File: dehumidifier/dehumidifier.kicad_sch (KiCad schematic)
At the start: 13 parts, among them J1 Conn_01x04_Pin, J2 Conn_01x02_Pin, J3 Conn_01x03_Pin, J4 Conn_01x03_Pin, J5 Barrel_Jack_Switch, M1 Fan, Q1 Q_NMOS_GDS, U1 SeeeduinoXIAO, U2 DHT11, U3 DS18B20

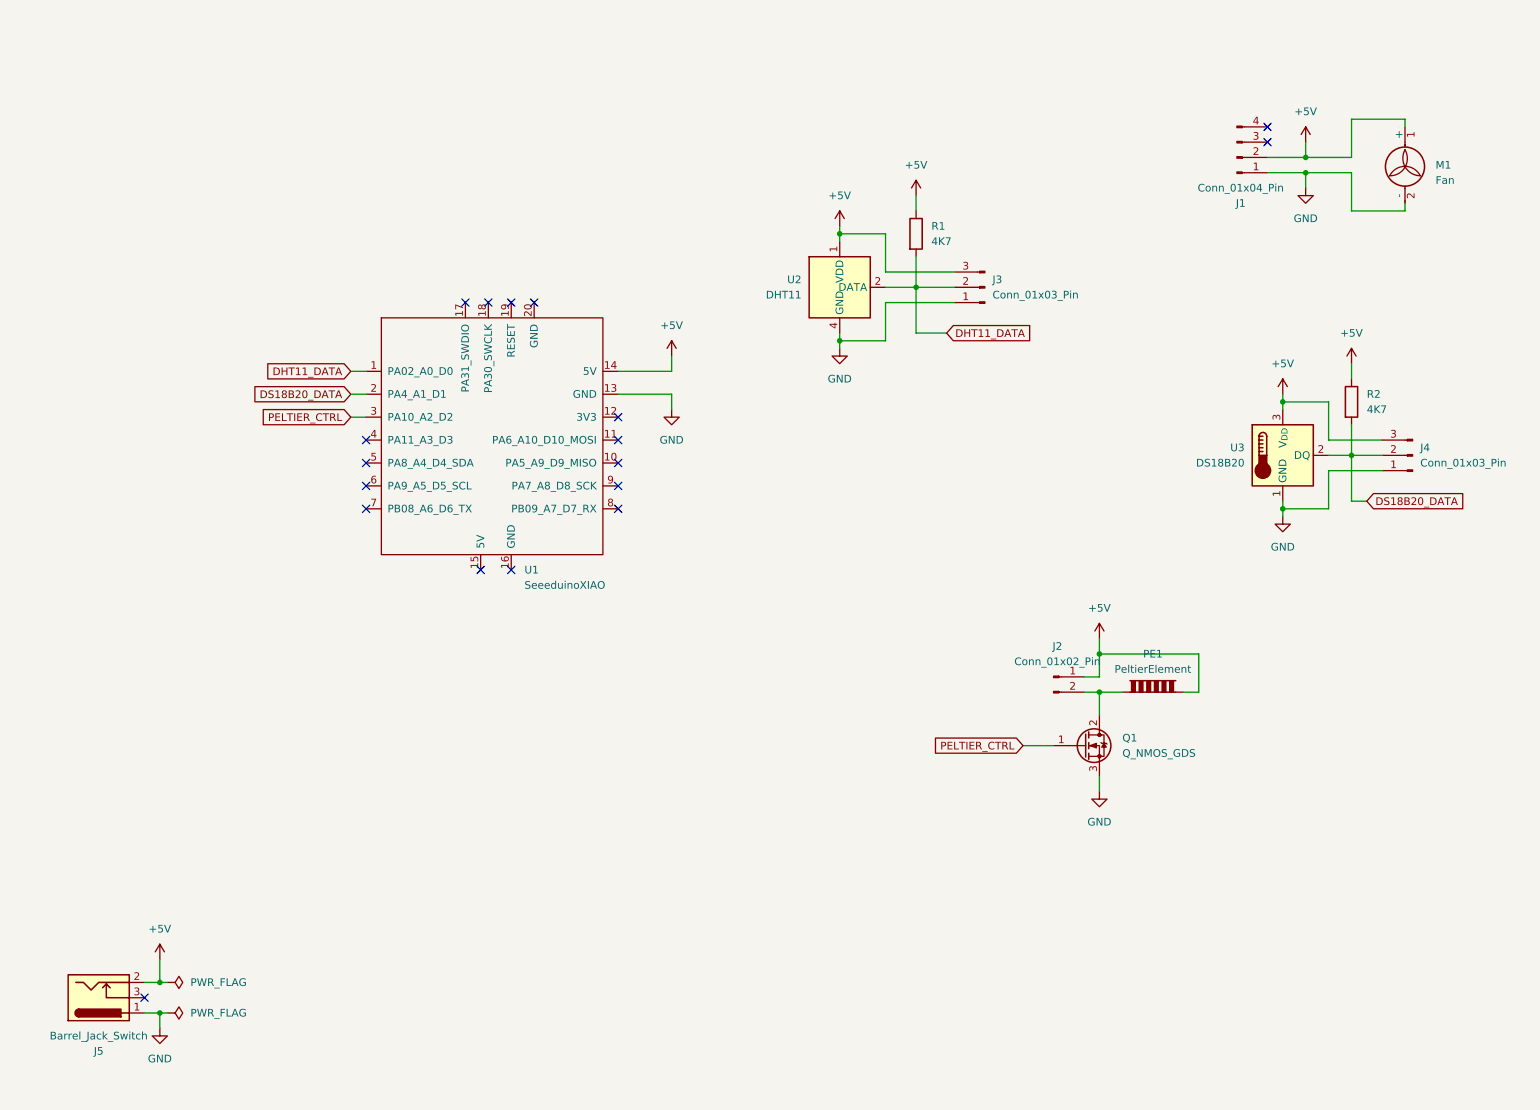
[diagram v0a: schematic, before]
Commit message: fix power connector
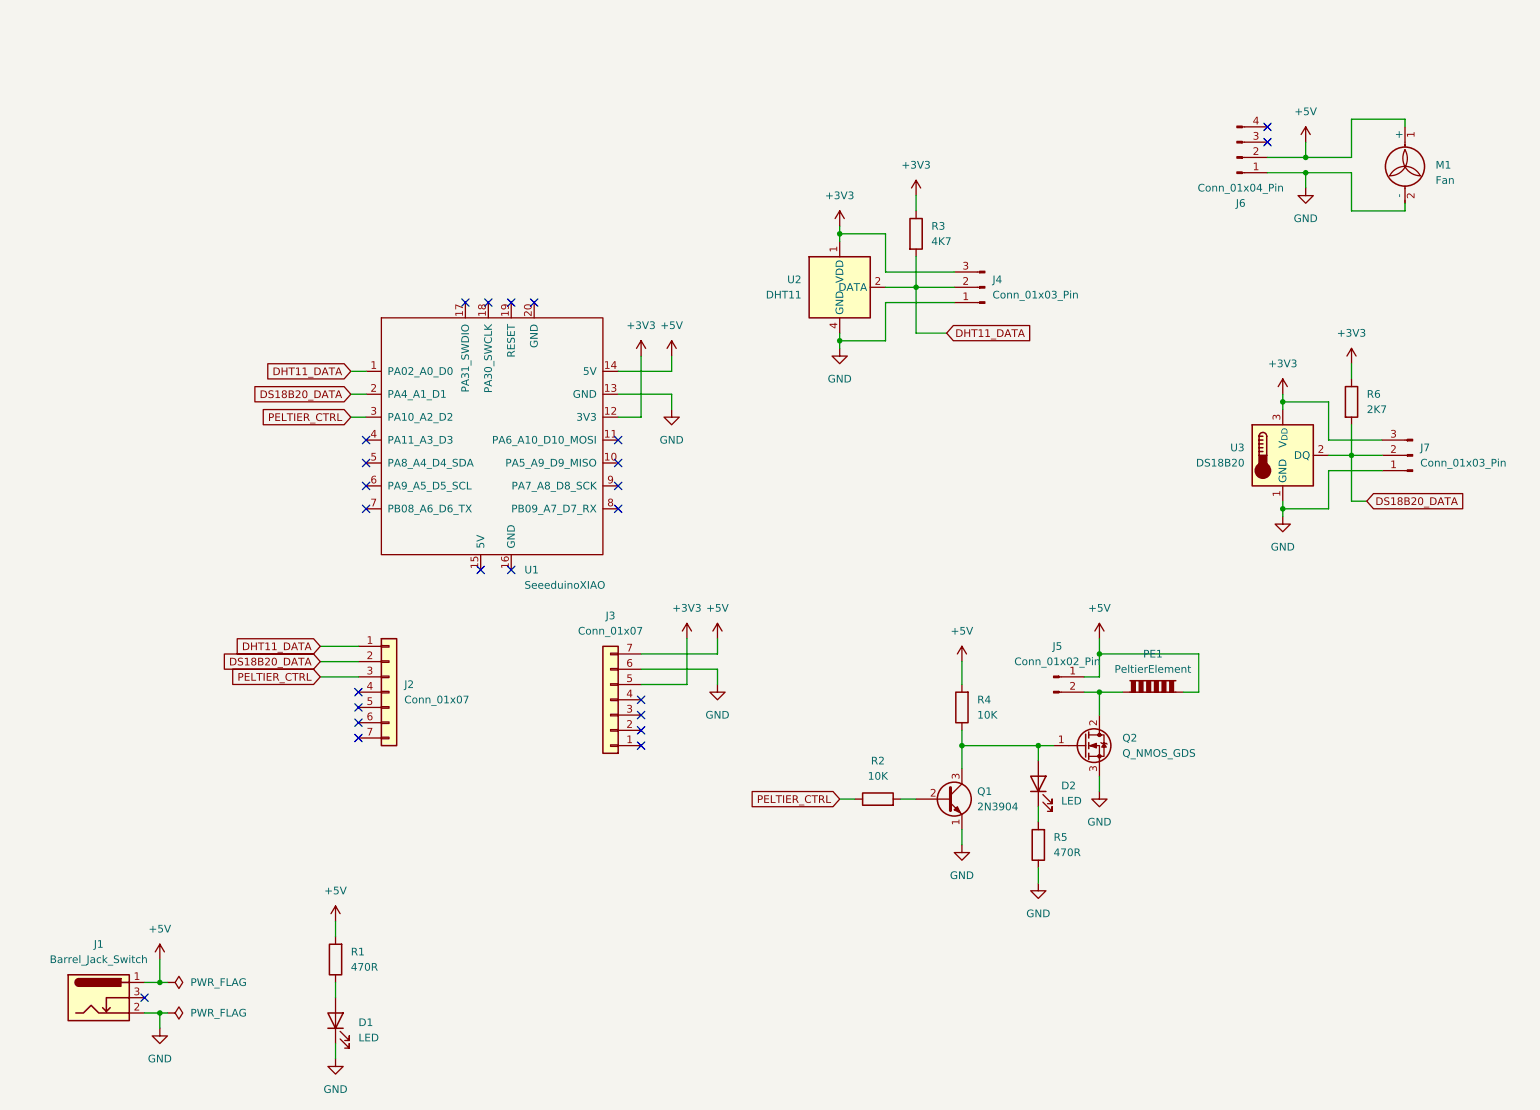
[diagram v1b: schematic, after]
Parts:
- added D1, D2: LED, LED_THT:LED_D3.0mm, symbol Device:LED
- added J2, J3: Conn_01x07, Connector_PinHeader_2.54mm:PinHeader_1x07_P2.54mm_Vertical, symbol Connector_Generic:Conn_01x07
- added Q1: 2N3904, Package_TO_SOT_THT:TO-92_HandSolder, symbol Transistor_BJT:2N3904
- added R1, R5: 470R, Resistor_THT:R_Axial_DIN0207_L6.3mm_D2.5mm_P7.62mm_Horizontal, symbol Device:R
- added R2, R4: 10K, Resistor_THT:R_Axial_DIN0207_L6.3mm_D2.5mm_P7.62mm_Horizontal, symbol Device:R
- R6: renamed from R2; value 4K7 -> 2K7
- renumbered J5 to J1, J3 to J4, J2 to J5, J1 to J6, J4 to J7, Q1 to Q2, R1 to R3
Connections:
- net +5V: now also J1.1, J3.7 (Pin_7), R1.2, R4.2; no longer J1.2, J4.3 (Pin_3), J7.3 (Pin_3), R3.1, R6.1, U2.1 (VDD), U3.3 (V_{DD})
- net DHT11_DATA: now also J2.1 (Pin_1)
- net DS18B20_DATA: now also J2.2 (Pin_2)
- net GND: now also J1.2, D1.1 (K), J3.6 (Pin_6), Q1.1 (E), R5.1; no longer J1.1
- net PELTIER_CTRL: now also J2.3 (Pin_3), R2.1; no longer Q2.1 (G)
- net +3V3: now reaches U1.12 (3V3)
- net +3V3: now also J4.3 (Pin_3), J7.3 (Pin_3), R3.1, R6.1, U2.1 (VDD), U3.3 (V_{DD}), J3.5 (Pin_5)
- new net: D2.2 (A), Q1.3 (C), Q2.1 (G), R4.1
- new net: Q1.2 (B), R2.2
- new net: D2.1 (K), R5.2
- new net: D1.2 (A), R1.1
- no-connect marks 18 -> 25

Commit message: adding current sensing
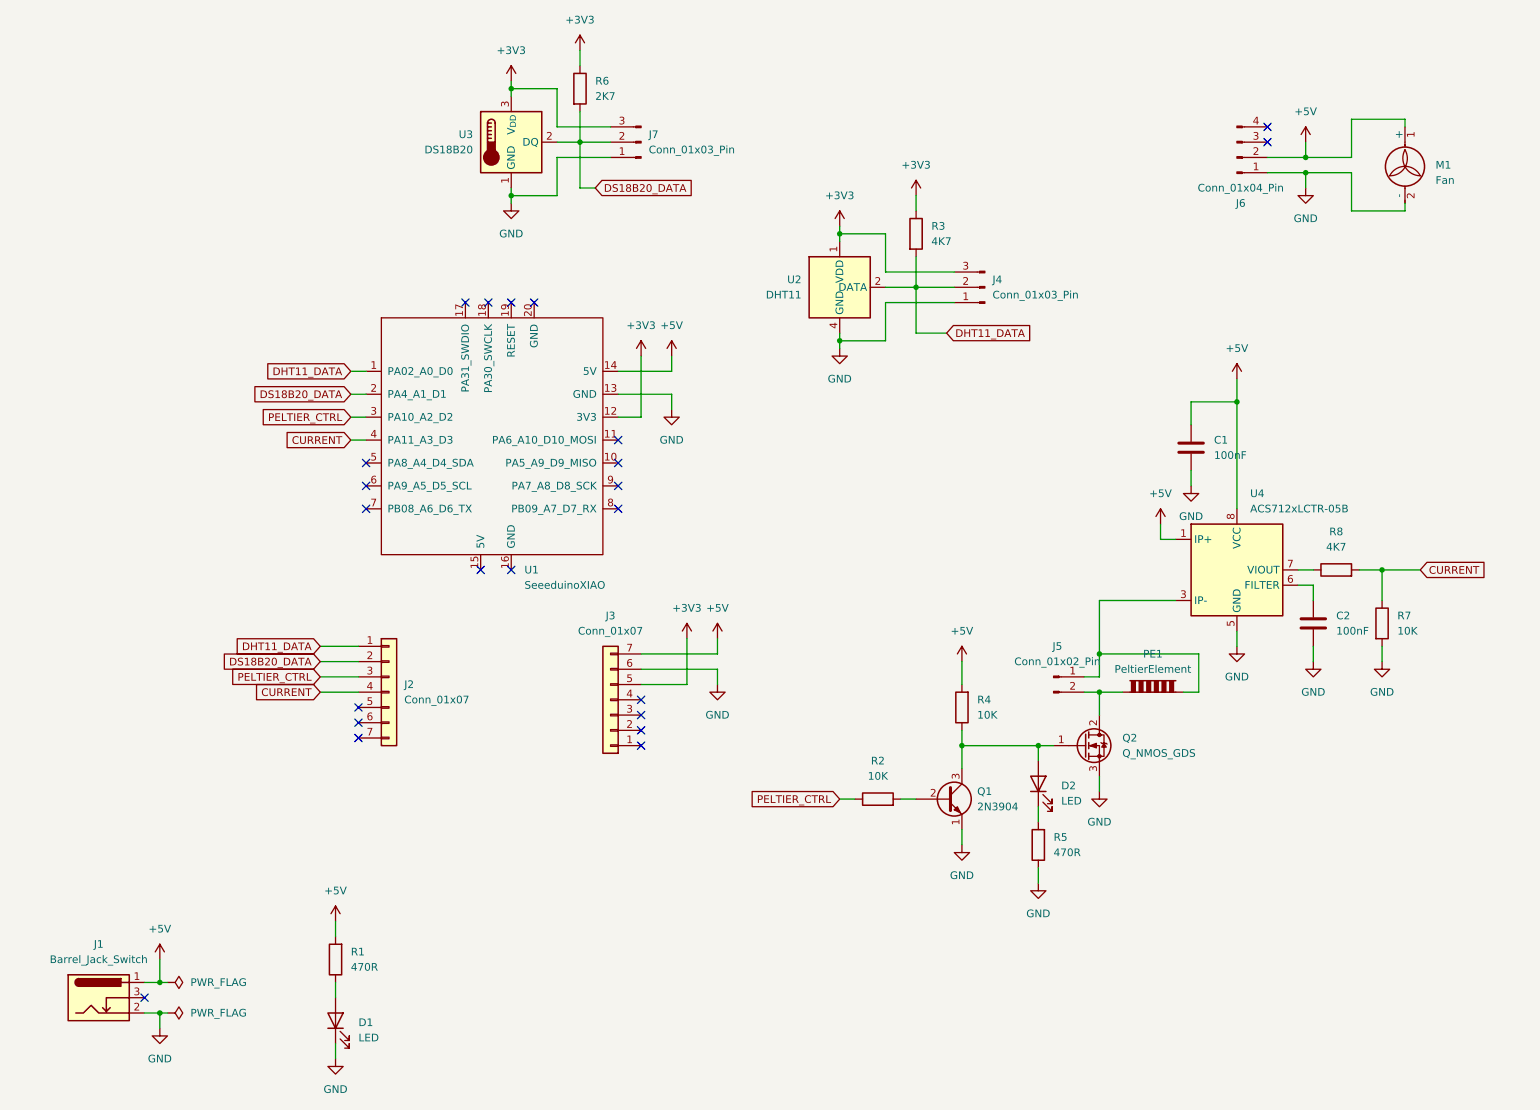
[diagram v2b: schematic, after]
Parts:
- added C1, C2: 100nF, Capacitor_THT:C_Disc_D3.0mm_W1.6mm_P2.50mm, symbol Device:C
- added R7: 10K, Resistor_THT:R_Axial_DIN0207_L6.3mm_D2.5mm_P7.62mm_Horizontal, symbol Device:R
- added R8: 4K7, Resistor_THT:R_Axial_DIN0207_L6.3mm_D2.5mm_P7.62mm_Horizontal, symbol Device:R
- added U4: ACS712xLCTR-05B, Package_SO:SOIC-8_3.9x4.9mm_P1.27mm, symbol Sensor_Current:ACS712xLCTR-05B
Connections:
- net +5V: now also C1.1, U4.1 (IP+), U4.2 (IP+), U4.8 (VCC); no longer J5.1 (Pin_1), PE1.2
- net GND: now also C1.2, C2.2, R7.2, U4.5 (GND)
- net CURRENT: now reaches U1.4 (PA11_A3_D3)
- net CURRENT: now also J2.4 (Pin_4), R7.1, R8.2
- new net: J5.1 (Pin_1), PE1.2, U4.3 (IP-), U4.4 (IP-)
- new net: C2.1, U4.6 (FILTER)
- new net: R8.1, U4.7 (VIOUT)
- no-connect marks 25 -> 23
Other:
- moved on the sheet: J7, R6, U3

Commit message: 12V for peltier
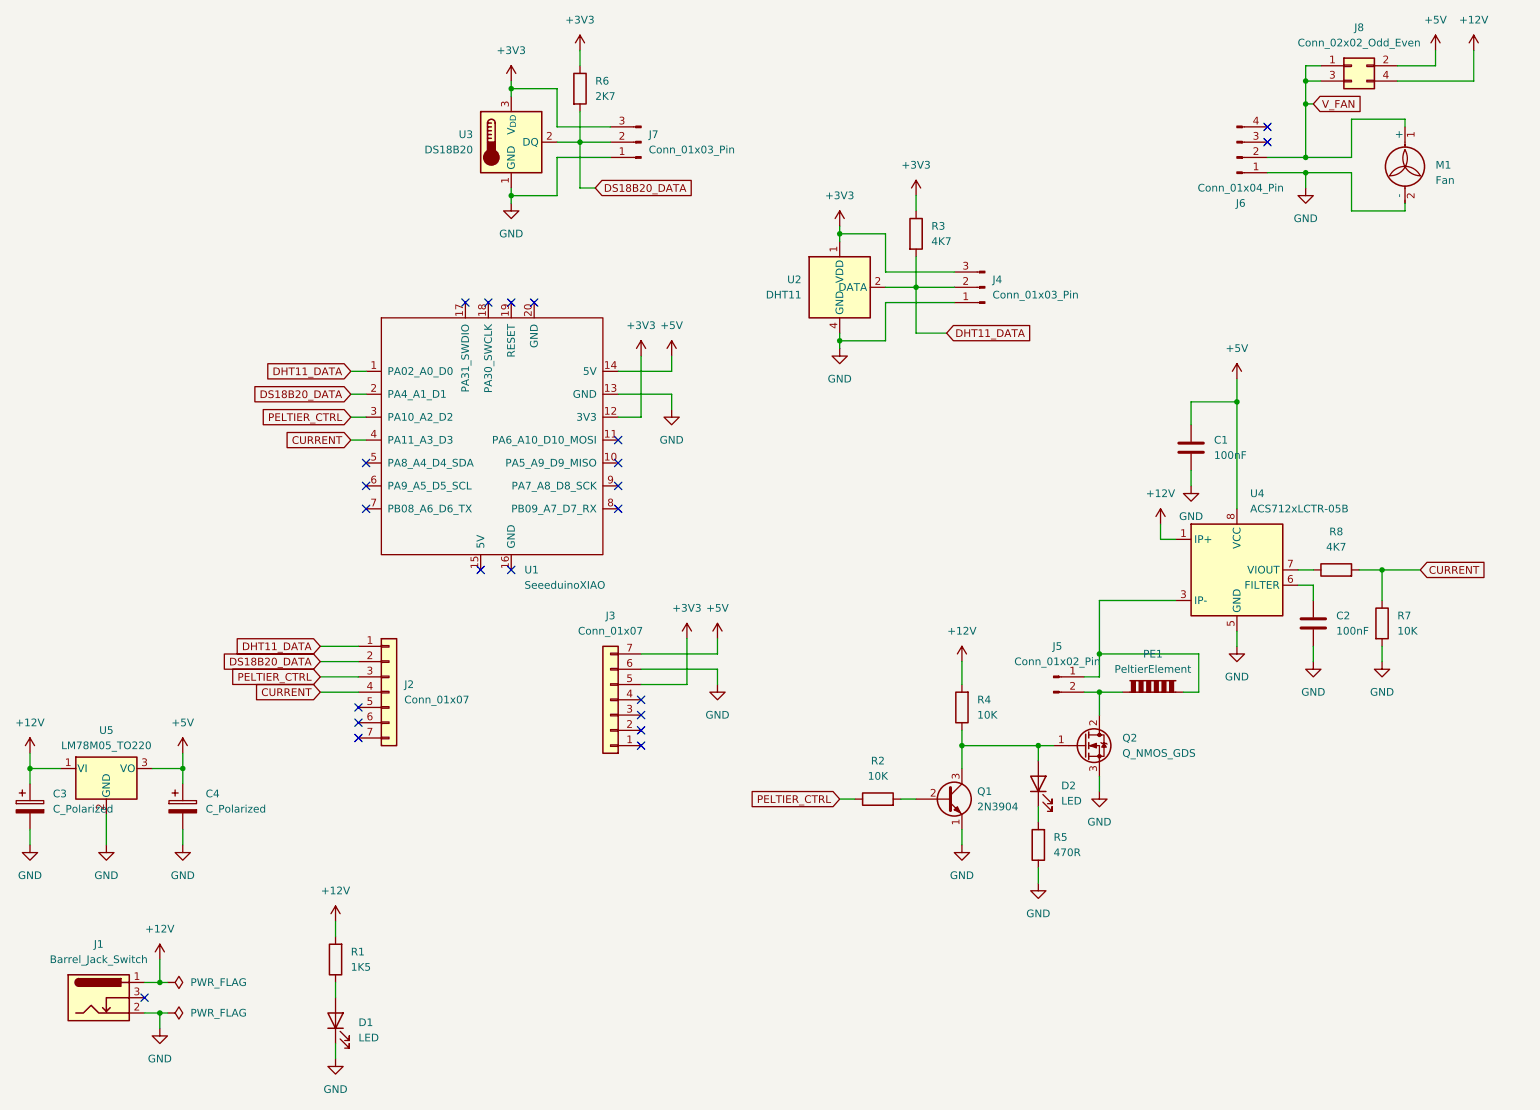
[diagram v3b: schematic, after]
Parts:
- added C3, C4: C_Polarized, Capacitor_THT:CP_Radial_D6.3mm_P2.50mm, symbol Device:C_Polarized
- added J8: Conn_02x02_Odd_Even, Connector_PinHeader_2.54mm:PinHeader_2x02_P2.54mm_Vertical, symbol Connector_Generic:Conn_02x02_Odd_Even
- added U5: LM78M05_TO220, Package_TO_SOT_THT:TO-220-3_Vertical, symbol Regulator_Linear:LM78M05_TO220
- R1: value 470R -> 1K5
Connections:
- net +5V: now also C4.1, J8.2 (Pin_2), U5.3 (VO); no longer J1.1, J6.2 (Pin_2), M1.1 (+), R1.2, R4.2, U4.1 (IP+), U4.2 (IP+)
- net GND: now also C3.2, C4.2, U5.2 (GND)
- new net +12V: C3.1, J1.1, J8.4 (Pin_4), R1.2, R4.2, U4.1 (IP+), U4.2 (IP+), U5.1 (VI)
- new net V_FAN: J6.2 (Pin_2), J8.1 (Pin_1), J8.3 (Pin_3), M1.1 (+)
